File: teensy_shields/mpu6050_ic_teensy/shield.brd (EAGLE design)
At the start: 26.6 x 60.6 mm, 6 parts

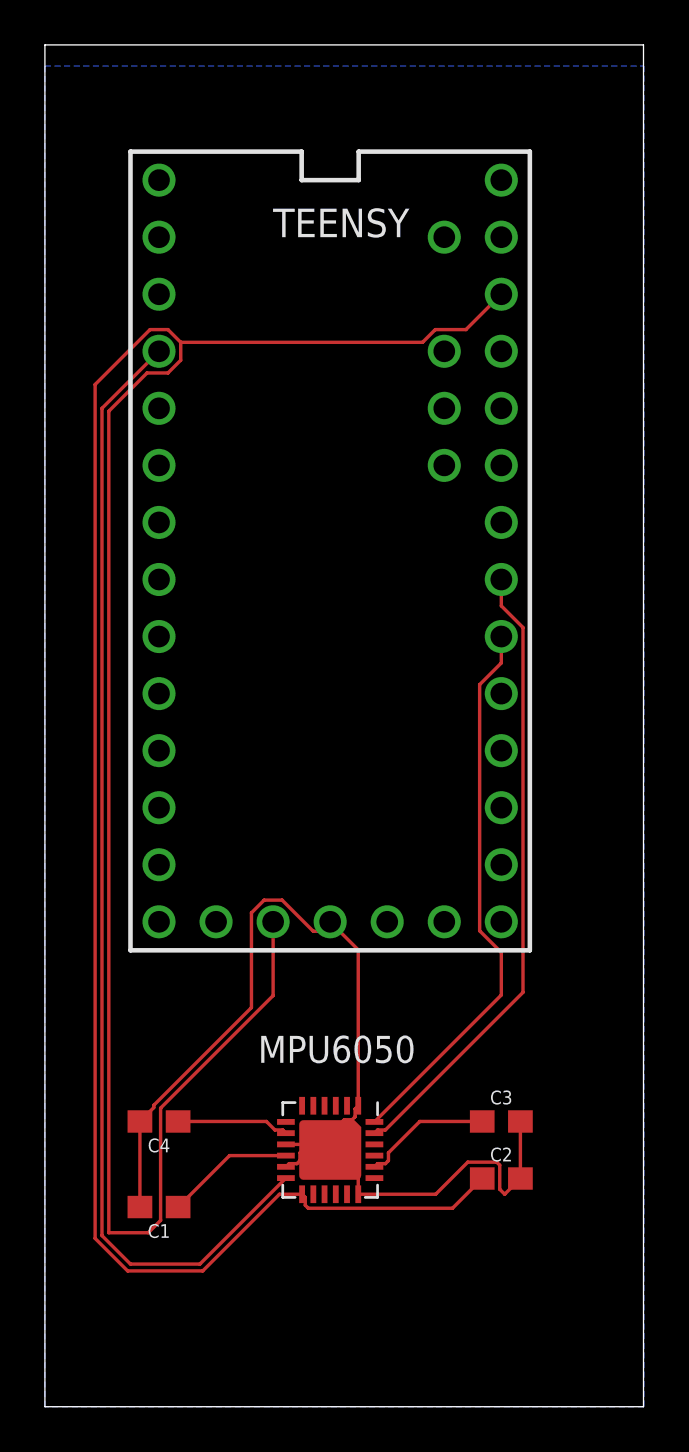
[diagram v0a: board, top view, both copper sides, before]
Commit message: components moved, via example, design version/credit
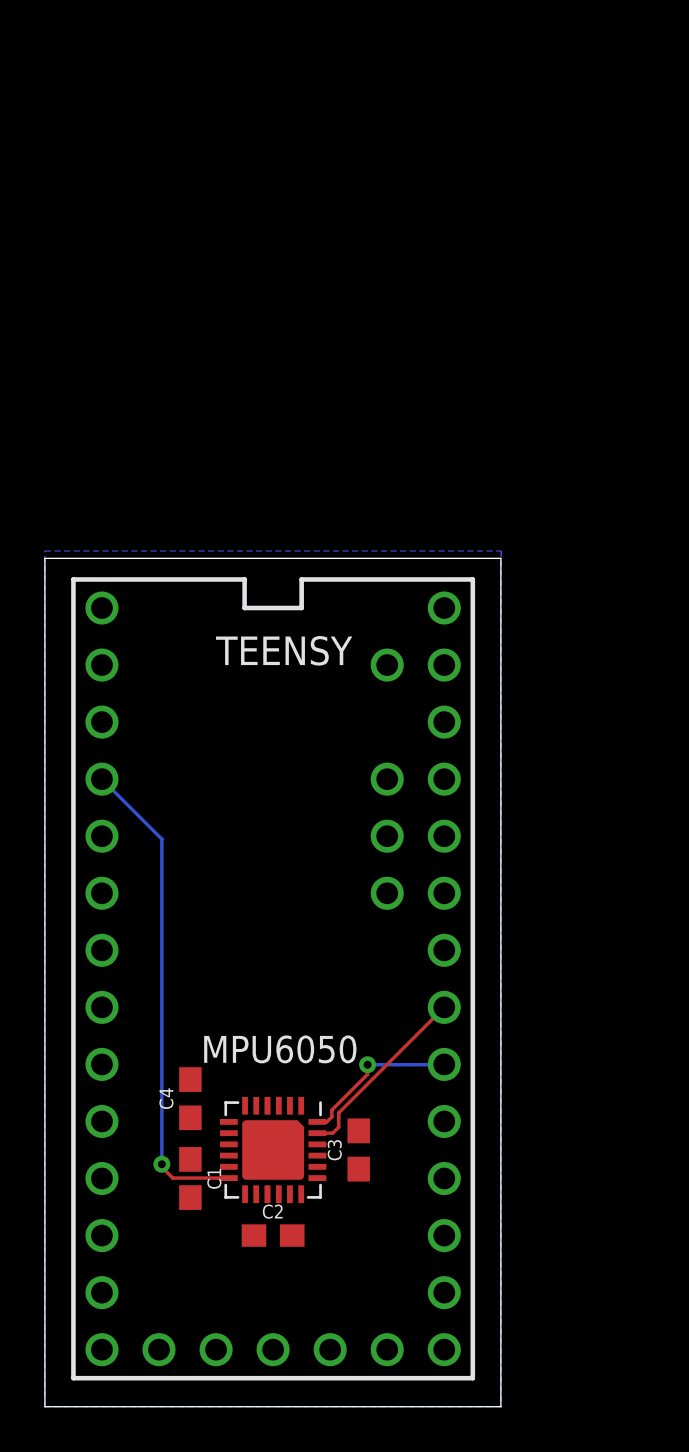
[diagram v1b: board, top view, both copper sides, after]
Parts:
- moved TEENSY 19.2 mm to (15.2, 58.4)
- moved C2 10.5 mm to (15.2, 47.0)
- moved C3 6.48 mm to (19.1, 50.8), turned to 90 degrees
- moved MPU6050 2.54 mm to (15.2, 50.8)
- moved C1 1.89 mm to (11.6, 49.5), turned to 270 degrees
- moved C4 1.73 mm to (11.6, 53.1), turned to 90 degrees
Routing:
- net VCC: track 137.9 -> 0.00 mm
- net GND: track 50.5 -> 0.00 mm
- net INT: track 50.7 -> 21.6 mm, vias 0 -> 1
- net SCL: track 28.0 -> 8.34 mm
- net SDA: track 24.7 -> 7.14 mm, vias 0 -> 1
- net N$1: track 5.84 -> 0.00 mm
- net N$2: track 5.75 -> 0.00 mm
- net N$3: track 5.02 -> 0.00 mm
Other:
- board size 26.6 x 60.6 mm -> 20.3 x 37.8 mm
- board text added: "MPU6050 Teensy Shield Oct. 6, 2018 Designed by Jack Proudfoot"
